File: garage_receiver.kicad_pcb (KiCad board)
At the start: 2 copper layers, 11 parts, among them J1 Conn_01x04_Female, J2 Screw_Terminal_01x04, Q1 2N7002, SW1 SW_DIP_x08, U1 HT12D

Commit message: DC/DC Converter Controller
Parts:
- removed C1: 470u, Capacitor_THT:CP_Radial_D10.0mm_P5.00mm
- removed D1, D2, D3, D4: 1N4007, Diode_THT:D_DO-41_SOD81_P10.16mm_Horizontal
- removed J1: Conn_01x04_Female, Connector_PinSocket_2.54mm:PinSocket_1x04_P2.54mm_Vertical
- removed J2: Screw_Terminal_01x04, TerminalBlock_RND:TerminalBlock_RND_205-00003_1x04_P5.00mm_Horizontal
- removed Q1: 2N7002, Package_TO_SOT_SMD:SOT-23
- removed R1: 47k, Resistor_SMD:R_0805_2012Metric
- removed SW1: SW_DIP_x08, Button_Switch_THT:SW_DIP_SPSTx08_Slide_9.78x22.5mm_W7.62mm_P2.54mm
- removed U1: HT12D, Package_SO:SOIC-20W_7.5x12.8mm_P1.27mm
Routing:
- net Net-(SW1-Pad9): track 8.76 -> 0.00 mm
- net Net-(SW1-Pad10): track 8.23 -> 0.00 mm
- net Net-(SW1-Pad11): track 7.70 -> 0.00 mm
- net Net-(SW1-Pad16): track 7.66 -> 0.00 mm
- net Net-(SW1-Pad12): track 7.18 -> 0.00 mm
- net Net-(SW1-Pad15): track 7.13 -> 0.00 mm
- net Net-(SW1-Pad14): track 6.79 -> 0.00 mm
- net Net-(SW1-Pad13): track 6.74 -> 0.00 mm
- net Net-(D2-Pad2): track 5.08 -> 0.00 mm
- net Net-(R1-Pad2): track 3.53 -> 0.00 mm
- net Net-(R1-Pad1): track 3.49 -> 0.00 mm

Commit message: PCB Layout
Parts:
- added C1: 470u, Capacitor_THT:CP_Radial_D10.0mm_P5.00mm, F.Cu at (207.0, 104.8)
- added C2: 47u, Capacitor_THT:CP_Radial_D5.0mm_P2.00mm, F.Cu at (217.2, 91.2)
- added C3: 2.2u, Capacitor_THT:C_Disc_D4.3mm_W1.9mm_P5.00mm, F.Cu at (211.3, 86.1)
- added C4: 1u, Capacitor_THT:CP_Radial_D4.0mm_P1.50mm, F.Cu at (214.9, 100.1)
- added D1: 1N4007, Diode_THT:D_DO-41_SOD81_P10.16mm_Horizontal, F.Cu at (194.3, 107.3)
- added D2: 1N4007, Diode_THT:D_DO-41_SOD81_P10.16mm_Horizontal, F.Cu at (190.5, 97.2)
- added D3: 1N4007, Diode_THT:D_DO-41_SOD81_P10.16mm_Horizontal, F.Cu at (198.1, 97.2)
- added D4: 1N4007, Diode_THT:D_DO-41_SOD81_P10.16mm_Horizontal, F.Cu at (201.9, 107.3)
- added J1: Conn_01x04_Female, Connector_PinSocket_2.54mm:PinSocket_1x04_P2.54mm_Vertical, F.Cu at (230.6, 86.9)
- added J2: Screw_Terminal_01x04, TerminalBlock_RND:TerminalBlock_RND_205-00003_1x04_P5.00mm_Horizontal, F.Cu at (207.0, 90.2)
- added L1: 33u, Inductor_SMD:L_10.4x10.4_H4.8, F.Cu at (222.8, 98.8)
- added Q1: 2N7002, Package_TO_SOT_SMD:SOT-23, F.Cu at (205.7, 97.8)
- added R1: 100k, Resistor_SMD:R_0805_2012Metric, F.Cu at (211.8, 94.5)
- added R2: 1k, Resistor_SMD:R_0805_2012Metric, F.Cu at (204.5, 109.9)
- added R3: 47k, Resistor_SMD:R_0805_2012Metric, F.Cu at (227.3, 90.9)
- added R4: 100k, Resistor_SMD:R_0805_2012Metric, F.Cu at (214.9, 95.0)
- added R5: 10k, Resistor_SMD:R_0805_2012Metric, F.Cu at (211.3, 91.4)
- added R6: 2k, Resistor_SMD:R_0805_2012Metric, F.Cu at (213.4, 91.4)
- added SW1: SW_DIP_x08, Button_Switch_THT:SW_DIP_SPSTx08_Slide_9.78x22.5mm_W7.62mm_P2.54mm, F.Cu at (217.9, 113.8)
- added U1: HT12D, Package_SO:SOIC-20W_7.5x12.8mm_P1.27mm, F.Cu at (235.2, 95.0)
- added U2: MP1470, Package_TO_SOT_SMD:TSOT-23-6, F.Cu at (210.3, 97.5)
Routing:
- net /open: track 0.00 -> 34.1 mm, vias 0 -> 2
- net +12V: track 0.00 -> 20.9 mm
- net Net-(SW1-Pad16): track 0.00 -> 17.7 mm, vias 0 -> 1
- net Net-(C4-Pad1): track 0.00 -> 17.0 mm
- net Net-(SW1-Pad15): track 0.00 -> 16.8 mm, vias 0 -> 1
- net +5V: track 0.00 -> 16.8 mm, vias 0 -> 2
- net GNDPWR: track 0.00 -> 16.5 mm
- net VAC: track 0.00 -> 15.5 mm
- net Net-(D1-Pad1): track 0.00 -> 15.1 mm
- net Net-(SW1-Pad14): track 0.00 -> 14.3 mm
- net Net-(SW1-Pad13): track 0.00 -> 12.7 mm
- net /rf_data: track 0.00 -> 12.4 mm
- net Net-(SW1-Pad12): track 0.00 -> 11.1 mm
- net Net-(SW1-Pad11): track 0.00 -> 9.84 mm
- net Net-(R3-Pad2): track 0.00 -> 8.89 mm
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- added copper zone on B.Cu, net +5V
- added copper zone on F.Cu, net GND
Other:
- board outline added: 54.6 x 31.8 mm
- net class 12V added: clearance 0.2, trace_width 0.6, via_dia 0.8, via_drill 0.4
- net class AC added: clearance 0.2, trace_width 1.5, via_dia 0.8, via_drill 0.4
- net class Default: trace_width 0.4 -> 0.3
- rule trace_min: 0.2 -> 0.15
- board text added: "24AC"
- board text added: "C1"
- board text added: "C2"
- board text added: "Designed by:"
- board text added: "GND"
- board text added: "Gonçalo Pereira"
- board text added: "Sources at: https://github.com/G-Pereira/garage_receiver"

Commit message: Prepare for production
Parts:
- added H1: MountingHole, MountingHole:MountingHole_3.2mm_M3, F.Cu at (178.5, 82.2)
- added H2: MountingHole, MountingHole:MountingHole_3.2mm_M3, F.Cu at (253.5, 82.2)
- added H3: MountingHole, MountingHole:MountingHole_3.2mm_M3, F.Cu at (178.5, 117.2)
- added H4: MountingHole, MountingHole:MountingHole_3.2mm_M3, F.Cu at (253.5, 117.2)
- moved C1 0.64 mm to (207.5, 104.4)
- moved C2 0.64 mm to (217.7, 90.8)
- moved C3 0.64 mm to (211.8, 85.7)
- moved C4 0.64 mm to (215.4, 99.7)
- moved D1 0.64 mm to (194.8, 106.9)
- moved D2 0.64 mm to (191.0, 96.8)
- moved J2 0.64 mm to (207.5, 89.8)
- moved R2 0.64 mm to (205.0, 109.5)
- moved R4 0.64 mm to (215.4, 94.6)
- moved R5 0.64 mm to (211.8, 91.1)
- moved SW1 0.64 mm to (218.4, 113.4)
- moved D3 0.63 mm to (198.6, 96.8)
- moved D4 0.63 mm to (202.4, 106.9)
- moved J1 0.63 mm to (231.1, 86.5)
- moved L1 0.63 mm to (223.3, 98.4)
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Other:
- board size 54.6 x 31.8 mm -> 85 x 45 mm
- rule trace_min: 0.15 -> 0.2
- board text added: "5V"
- board text added: "DATA"
- board text added: "Garage Receiver"
- board text added: "RF Receiver 433/315MHz"
- board text added: "https://github.com/G-Pereira/garage_receiver"
- board text added: "v1.0.0"
- board text removed: "Designed by:"
- board text removed: "Gonçalo Pereira"
- board text removed: "Sources at: https://github.com/G-Pereira/garage_receiver"

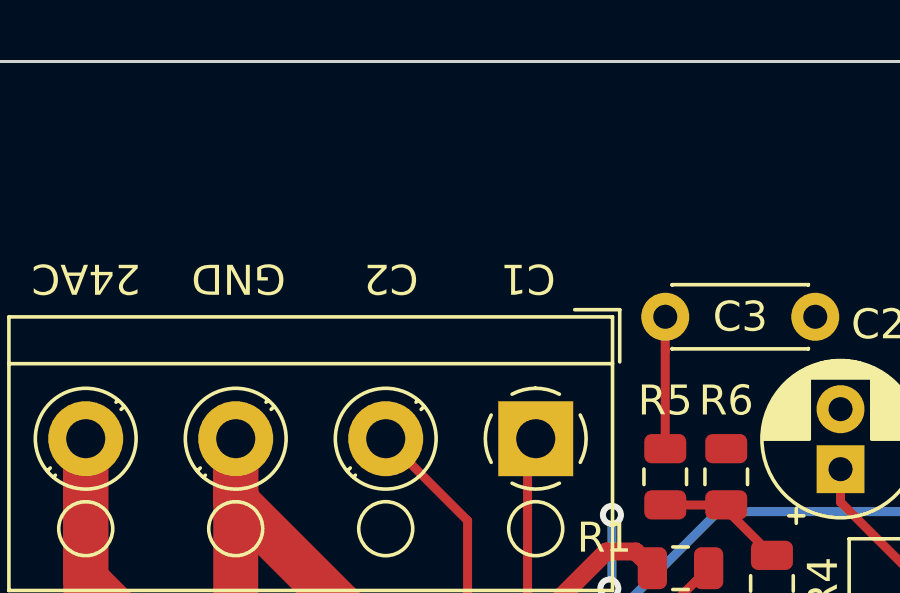
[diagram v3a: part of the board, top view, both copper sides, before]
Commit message: Change Control Pin Labels
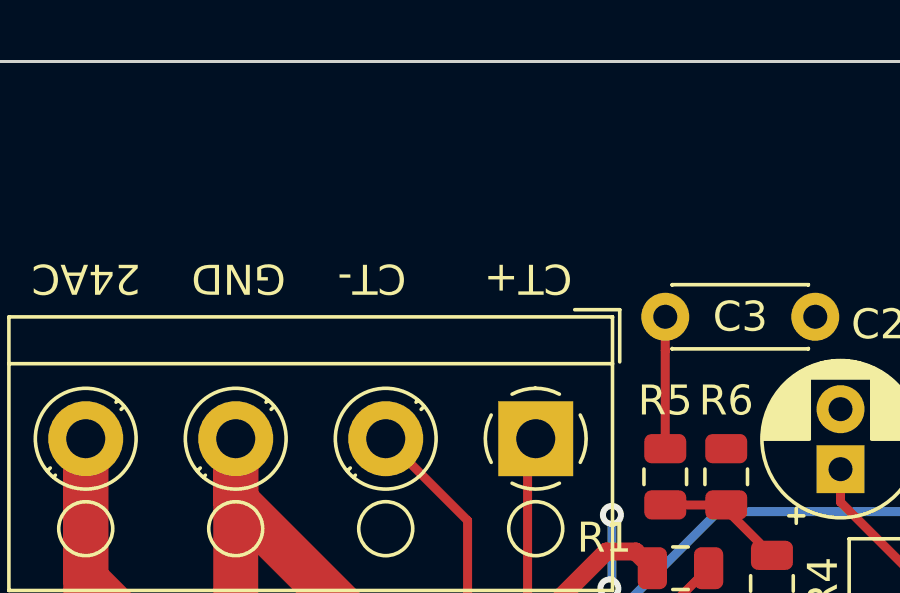
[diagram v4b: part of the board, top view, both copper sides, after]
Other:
- board text added: "CT+"
- board text added: "CT-"
- board text removed: "C1"
- board text removed: "C2"
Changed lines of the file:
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@@
     (effects (font (size 1 1) (thickness 0.15) italic))
   )
-  (gr_text C1 (at 207.264 84.455 180) (layer F.SilkS)
+  (gr_text CT+ (at 207.264 84.455 180) (layer F.SilkS)
     (effects (font (size 1 1) (thickness 0.15)))
   )
-  (gr_text C2 (at 202.692 84.455 180) (layer F.SilkS)
+  (gr_text CT- (at 202.057 84.455 180) (layer F.SilkS)
     (effects (font (size 1 1) (thickness 0.15)))
   )

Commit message: Rotate Labels
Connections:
- J2 pad 1: /door_control2 -> GND
- Q1 pad 2: /door_control2 -> GND
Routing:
- net /door_control2: track 6.78 -> 0.00 mm

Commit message: Fix PCB files
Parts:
- L1: moved to B.Cu
- turned L1 to 270 degrees
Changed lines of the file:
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@@
     )
   )
-  (module Inductor_SMD:L_10.4x10.4_H4.8 (layer F.Cu)
-    (at 223.266 98.425 90)
+  (module Inductor_SMD:L_10.4x10.4_H4.8 (layer B.Cu)
+    (at 223.266 98.425 270)
     (descr "Choke, SMD, 10.4x10.4mm 4.8mm height")
     (tags "Choke SMD")
     (attr smd)
-    (fp_text reference L1 (at 0 -6.35 90) (layer F.SilkS)
-      (effects (font (size 1 1) (thickness 0.15)))
-    )
-    (fp_text value 33u (at 0 6.35 90) (layer F.Fab)
-      (effects (font (size 1 1) (thickness 0.15)))
-    )
-    (fp_arc (start 0 0) (end -3.17 -3.17) (angle 90) (layer F.Fab) (width 0.1))
-    (fp_arc (start 0 0) (end 3.17 3.17) (angle 90) (layer F.Fab) (width 0.1))
-    (fp_line (start -5.2 5.2) (end 5.2 5.2) (layer F.Fab) (width 0.1))
-    (fp_line (start -5.2 -5.2) (end 5.2 -5.2) (layer F.Fab) (width 0.1))
-    (fp_line (start -5.2 5.2) (end -5.2 2.1) (layer F.Fab) (width 0.1))
-    (fp_line (start 5.2 5.2) (end 5.2 2.1) (layer F.Fab) (width 0.1))
-    (fp_line (start -5.2 -5.2) (end -5.2 -2.1) (layer F.Fab) (width 0.1))
-    (fp_line (start 5.2 -5.2) (end 5.2 -2.1) (layer F.Fab) (width 0.1))
-    (fp_line (start 5.75 -5.45) (end -5.75 -5.45) (layer F.CrtYd) (width 0.05))
-    (fp_line (start 5.75 5.45) (end 5.75 -5.45) (layer F.CrtYd) (width 0.05))
-    (fp_line (start -5.75 5.45) (end 5.75 5.45) (layer F.CrtYd) (width 0.05))
-    (fp_line (start -5.75 -5.45) (end -5.75 5.45) (layer F.CrtYd) (width 0.05))
-    (fp_line (start 5.3 -5.3) (end 5.3 -2.1) (layer F.SilkS) (width 0.12))
-    (fp_line (start -5.3 -5.3) (end 5.3 -5.3) (layer F.SilkS) (width 0.12))
-    (fp_line (start -5.3 -2.1) (end -5.3 -5.3) (layer F.SilkS) (width 0.12))
-    (fp_line (start -5.3 5.3) (end -5.3 2.1) (layer F.SilkS) (width 0.12))
-    (fp_line (start 5.3 5.3) (end -5.3 5.3) (layer F.SilkS) (width 0.12))
-    (fp_line (start 5.3 2.1) (end 5.3 5.3) (layer F.SilkS) (width 0.12))
-    (fp_text user %R (at 0 0 90) (layer F.Fab)
-      (effects (font (size 1 1) (thickness 0.15)))
-    )
-    (pad 2 smd rect (at 4.15 0 90) (size 2.7 3.6) (layers F.Cu F.Paste F.Mask)
+    (fp_text reference L1 (at 0 6.35 270) (layer B.SilkS)
+      (effects (font (size 1 1) (thickness 0.15)) (justify mirror))
+    )
+    (fp_text value 33u (at 0 -6.35 270) (layer B.Fab)
+      (effects (font (size 1 1) (thickness 0.15)) (justify mirror))
+    )
+    (fp_arc (start 0 0) (end -3.17 3.17) (angle -90) (layer B.Fab) (width 0.1))
+    (fp_arc (start 0 0) (end 3.17 -3.17) (angle -90) (layer B.Fab) (width 0.1))
+    (fp_line (start -5.2 -5.2) (end 5.2 -5.2) (layer B.Fab) (width 0.1))
+    (fp_line (start -5.2 5.2) (end 5.2 5.2) (layer B.Fab) (width 0.1))
+    (fp_line (start -5.2 -5.2) (end -5.2 -2.1) (layer B.Fab) (width 0.1))
+    (fp_line (start 5.2 -5.2) (end 5.2 -2.1) (layer B.Fab) (width 0.1))
+    (fp_line (start -5.2 5.2) (end -5.2 2.1) (layer B.Fab) (width 0.1))
+    (fp_line (start 5.2 5.2) (end 5.2 2.1) (layer B.Fab) (width 0.1))
+    (fp_line (start 5.75 5.45) (end -5.75 5.45) (layer B.CrtYd) (width 0.05))
+    (fp_line (start 5.75 -5.45) (end 5.75 5.45) (layer B.CrtYd) (width 0.05))
+    (fp_line (start -5.75 -5.45) (end 5.75 -5.45) (layer B.CrtYd) (width 0.05))
+    (fp_line (start -5.75 5.45) (end -5.75 -5.45) (layer B.CrtYd) (width 0.05))
+    (fp_line (start 5.3 5.3) (end 5.3 2.1) (layer B.SilkS) (width 0.12))
+    (fp_line (start -5.3 5.3) (end 5.3 5.3) (layer B.SilkS) (width 0.12))
+    (fp_line (start -5.3 2.1) (end -5.3 5.3) (layer B.SilkS) (width 0.12))
+    (fp_line (start -5.3 -5.3) (end -5.3 -2.1) (layer B.SilkS) (width 0.12))
+    (fp_line (start 5.3 -5.3) (end -5.3 -5.3) (layer B.SilkS) (width 0.12))
+    (fp_line (start 5.3 -2.1) (end 5.3 -5.3) (layer B.SilkS) (width 0.12))
+    (fp_text user %R (at 0 0 270) (layer B.Fab)
+      (effects (font (size 1 1) (thickness 0.15)) (justify mirror))
+    )
+    (pad 2 smd rect (at 4.15 0 270) (size 2.7 3.6) (layers B.Cu B.Paste B.Mask)
       (net 3 +5V))
-    (pad 1 smd rect (at -4.15 0 90) (size 2.7 3.6) (layers F.Cu F.Paste F.Mask)
+    (pad 1 smd rect (at -4.15 0 270) (size 2.7 3.6) (layers B.Cu B.Paste B.Mask)
       (net 5 "Net-(C4-Pad1)"))
     (model ${KISYS3DMOD}/Inductor_SMD.3dshapes/L_10.4x10.4_H4.8.wrl
@@
   (via (at 210.058 92.329) (size 0.8) (drill 0.4) (layers F.Cu B.Cu) (net 1))
   (via (at 209.972169 94.783169) (size 0.8) (drill 0.4) (layers F.Cu B.Cu) (net 1))
+  (segment (start 207.248 90.059) (end 207.518 89.789) (width 0.3) (layer F.Cu) (net 1))
   (segment (start 210.850263 93.550763) (end 209.872573 93.550763) (width 0.6) (layer F.Cu) (net 2))
   (segment (start 205.9155 105.9965) (end 207.518 104.394) (width 1.5) (layer F.Cu) (net 2))
@@
   (segment (start 205.248 92.519) (end 202.518 89.789) (width 0.3) (layer F.Cu) (net 10))
   (segment (start 205.248 97.409) (end 205.248 92.519) (width 0.3) (layer F.Cu) (net 10))
-  (segment (start 207.248 90.059) (end 207.518 89.789) (width 0.3) (layer F.Cu) (net 1))
   (segment (start 232.137001 92.220999) (end 213.595001 92.220999) (width 0.3) (layer B.Cu) (net 11))
   (segment (start 205.867 99.949) (end 205.867 99.74) (width 0.3) (layer F.Cu) (net 11))

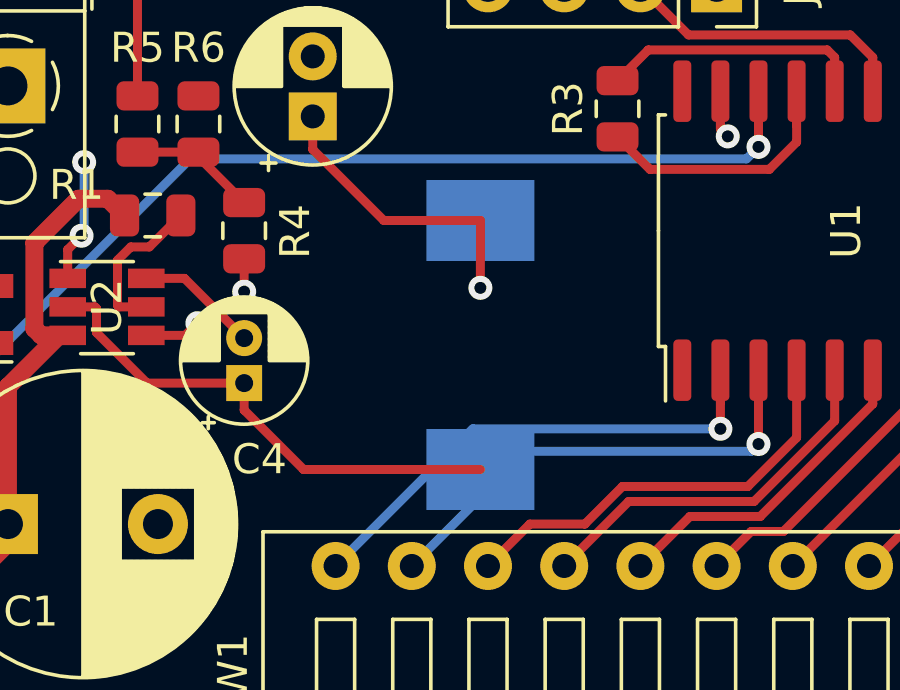
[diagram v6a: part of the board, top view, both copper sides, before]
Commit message: Fix Flipped Component
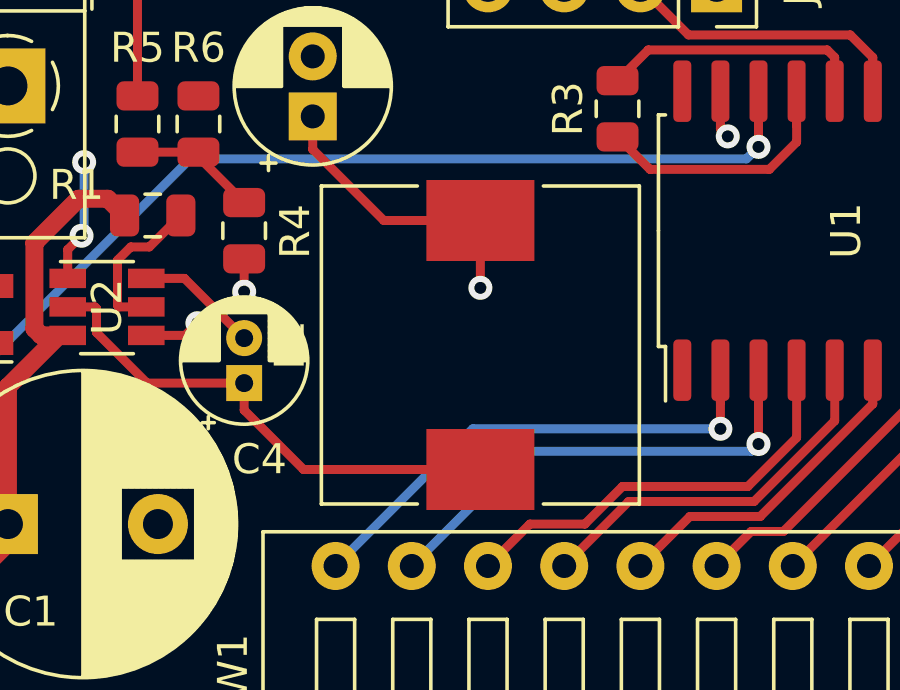
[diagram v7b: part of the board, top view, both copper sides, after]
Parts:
- L1: moved to F.Cu
- turned L1 to 90 degrees
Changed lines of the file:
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@@
     )
   )
-  (module Inductor_SMD:L_10.4x10.4_H4.8 (layer B.Cu)
-    (at 223.266 98.425 270)
+  (module Inductor_SMD:L_10.4x10.4_H4.8 (layer F.Cu)
+    (at 223.266 98.425 90)
     (descr "Choke, SMD, 10.4x10.4mm 4.8mm height")
     (tags "Choke SMD")
     (attr smd)
-    (fp_text reference L1 (at 0 6.35 270) (layer B.SilkS)
-      (effects (font (size 1 1) (thickness 0.15)) (justify mirror))
+    (fp_text reference L1 (at 0 -6.35 90) (layer F.SilkS)
+      (effects (font (size 1 1) (thickness 0.15)))
     )
-    (fp_text value 33u (at 0 -6.35 270) (layer B.Fab)
-      (effects (font (size 1 1) (thickness 0.15)) (justify mirror))
+    (fp_text value 33u (at 0 6.35 90) (layer F.Fab)
+      (effects (font (size 1 1) (thickness 0.15)))
     )
-    (fp_arc (start 0 0) (end -3.17 3.17) (angle -90) (layer B.Fab) (width 0.1))
-    (fp_arc (start 0 0) (end 3.17 -3.17) (angle -90) (layer B.Fab) (width 0.1))
-    (fp_line (start -5.2 -5.2) (end 5.2 -5.2) (layer B.Fab) (width 0.1))
-    (fp_line (start -5.2 5.2) (end 5.2 5.2) (layer B.Fab) (width 0.1))
-    (fp_line (start -5.2 -5.2) (end -5.2 -2.1) (layer B.Fab) (width 0.1))
-    (fp_line (start 5.2 -5.2) (end 5.2 -2.1) (layer B.Fab) (width 0.1))
-    (fp_line (start -5.2 5.2) (end -5.2 2.1) (layer B.Fab) (width 0.1))
-    (fp_line (start 5.2 5.2) (end 5.2 2.1) (layer B.Fab) (width 0.1))
-    (fp_line (start 5.75 5.45) (end -5.75 5.45) (layer B.CrtYd) (width 0.05))
-    (fp_line (start 5.75 -5.45) (end 5.75 5.45) (layer B.CrtYd) (width 0.05))
-    (fp_line (start -5.75 -5.45) (end 5.75 -5.45) (layer B.CrtYd) (width 0.05))
-    (fp_line (start -5.75 5.45) (end -5.75 -5.45) (layer B.CrtYd) (width 0.05))
-    (fp_line (start 5.3 5.3) (end 5.3 2.1) (layer B.SilkS) (width 0.12))
-    (fp_line (start -5.3 5.3) (end 5.3 5.3) (layer B.SilkS) (width 0.12))
-    (fp_line (start -5.3 2.1) (end -5.3 5.3) (layer B.SilkS) (width 0.12))
-    (fp_line (start -5.3 -5.3) (end -5.3 -2.1) (layer B.SilkS) (width 0.12))
-    (fp_line (start 5.3 -5.3) (end -5.3 -5.3) (layer B.SilkS) (width 0.12))
-    (fp_line (start 5.3 -2.1) (end 5.3 -5.3) (layer B.SilkS) (width 0.12))
-    (fp_text user %R (at 0 0 270) (layer B.Fab)
-      (effects (font (size 1 1) (thickness 0.15)) (justify mirror))
+    (fp_arc (start 0 0) (end -3.17 -3.17) (angle 90) (layer F.Fab) (width 0.1))
+    (fp_arc (start 0 0) (end 3.17 3.17) (angle 90) (layer F.Fab) (width 0.1))
+    (fp_line (start -5.2 5.2) (end 5.2 5.2) (layer F.Fab) (width 0.1))
+    (fp_line (start -5.2 -5.2) (end 5.2 -5.2) (layer F.Fab) (width 0.1))
+    (fp_line (start -5.2 5.2) (end -5.2 2.1) (layer F.Fab) (width 0.1))
+    (fp_line (start 5.2 5.2) (end 5.2 2.1) (layer F.Fab) (width 0.1))
+    (fp_line (start -5.2 -5.2) (end -5.2 -2.1) (layer F.Fab) (width 0.1))
+    (fp_line (start 5.2 -5.2) (end 5.2 -2.1) (layer F.Fab) (width 0.1))
+    (fp_line (start 5.75 -5.45) (end -5.75 -5.45) (layer F.CrtYd) (width 0.05))
+    (fp_line (start 5.75 5.45) (end 5.75 -5.45) (layer F.CrtYd) (width 0.05))
+    (fp_line (start -5.75 5.45) (end 5.75 5.45) (layer F.CrtYd) (width 0.05))
+    (fp_line (start -5.75 -5.45) (end -5.75 5.45) (layer F.CrtYd) (width 0.05))
+    (fp_line (start 5.3 -5.3) (end 5.3 -2.1) (layer F.SilkS) (width 0.12))
+    (fp_line (start -5.3 -5.3) (end 5.3 -5.3) (layer F.SilkS) (width 0.12))
+    (fp_line (start -5.3 -2.1) (end -5.3 -5.3) (layer F.SilkS) (width 0.12))
+    (fp_line (start -5.3 5.3) (end -5.3 2.1) (layer F.SilkS) (width 0.12))
+    (fp_line (start 5.3 5.3) (end -5.3 5.3) (layer F.SilkS) (width 0.12))
+    (fp_line (start 5.3 2.1) (end 5.3 5.3) (layer F.SilkS) (width 0.12))
+    (fp_text user %R (at 0 0 90) (layer F.Fab)
+      (effects (font (size 1 1) (thickness 0.15)))
     )
-    (pad 2 smd rect (at 4.15 0 270) (size 2.7 3.6) (layers B.Cu B.Paste B.Mask)
+    (pad 2 smd rect (at 4.15 0 90) (size 2.7 3.6) (layers F.Cu F.Paste F.Mask)
       (net 3 +5V))
-    (pad 1 smd rect (at -4.15 0 270) (size 2.7 3.6) (layers B.Cu B.Paste B.Mask)
+    (pad 1 smd rect (at -4.15 0 90) (size 2.7 3.6) (layers F.Cu F.Paste F.Mask)
       (net 5 "Net-(C4-Pad1)"))
     (model ${KISYS3DMOD}/Inductor_SMD.3dshapes/L_10.4x10.4_H4.8.wrl
